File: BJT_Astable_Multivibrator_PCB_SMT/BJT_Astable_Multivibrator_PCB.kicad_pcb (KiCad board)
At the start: 2 copper layers, 7 parts

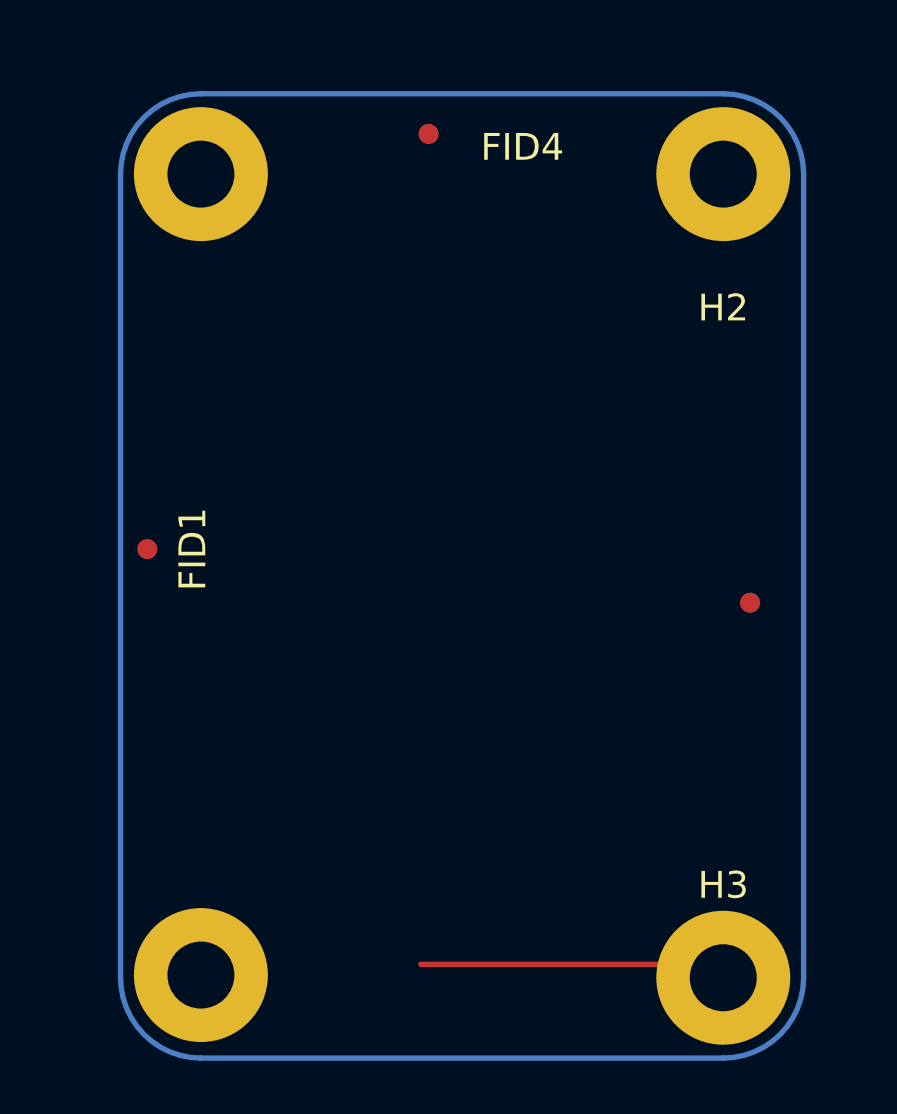
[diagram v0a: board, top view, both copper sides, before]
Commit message: added smt design of BJT mulitvibrator
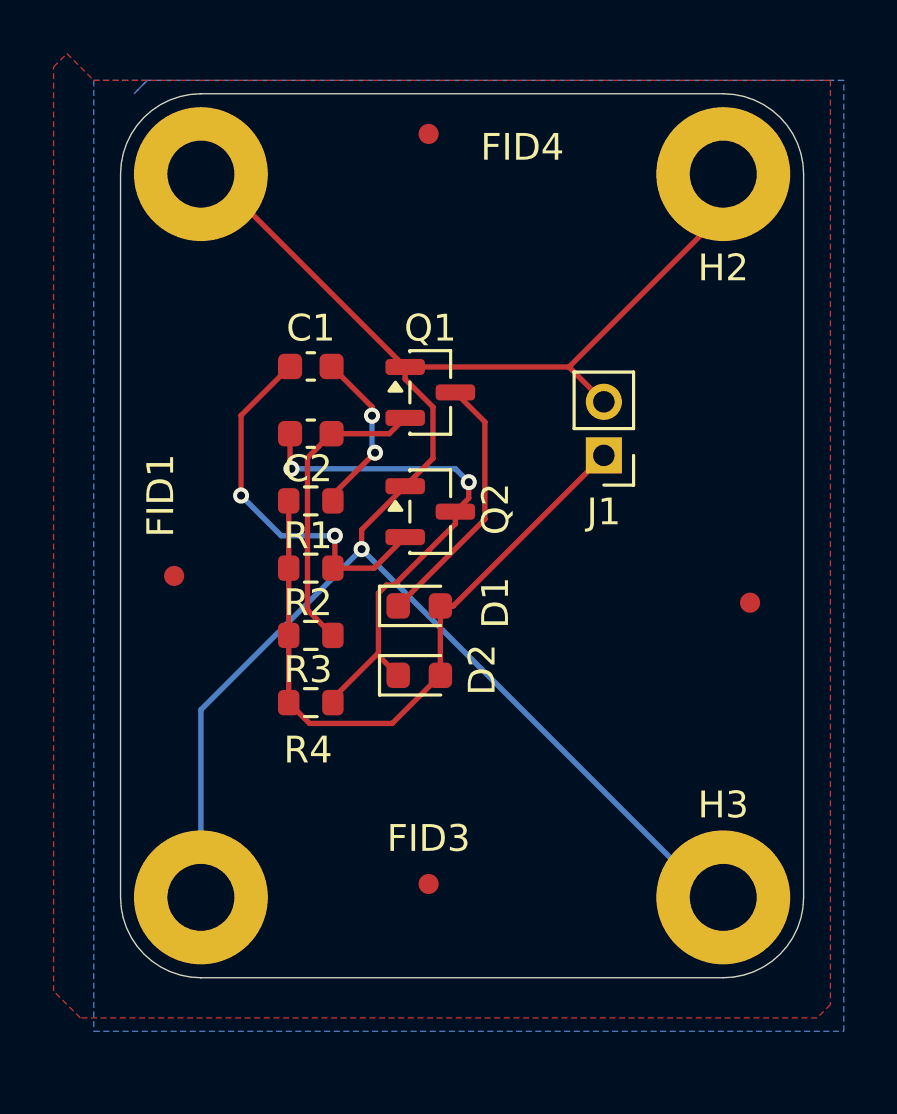
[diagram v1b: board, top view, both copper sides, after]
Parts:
- added C1: 220uF, Capacitor_SMD:C_0603_1608Metric, F.Cu at (150.6, 69.7)
- added C2: 220uF, Capacitor_SMD:C_0603_1608Metric, F.Cu at (150.6, 72.2)
- added D1: LED, LED_SMD:LED_0603_1608Metric, F.Cu at (154.7, 78.6)
- added D2: LED, LED_SMD:LED_0603_1608Metric, F.Cu at (154.7, 81.2)
- added FID3: Fiducial, Fiducial:Fiducial_0.75mm_Mask1.5mm, F.Cu at (155.0, 89.0)
- added J1: Conn_01x02_Pin, Connector_PinHeader_2.00mm:PinHeader_1x02_P2.00mm_Vertical, F.Cu at (161.5, 73.0)
- added Q1: 2N3904, Package_TO_SOT_SMD:SOT-23, F.Cu at (155.1, 70.7)
- added Q2: 2N3904, Package_TO_SOT_SMD:SOT-23, F.Cu at (155.1, 75.1)
- added R1: 1K, Resistor_SMD:R_0603_1608Metric, F.Cu at (150.6, 74.7)
- added R2: 5K, Resistor_SMD:R_0603_1608Metric, F.Cu at (150.6, 77.2)
- added R3: 5K, Resistor_SMD:R_0603_1608Metric, F.Cu at (150.6, 79.7)
- added R4: 1K, Resistor_SMD:R_0603_1608Metric, F.Cu at (150.6, 82.2)
- moved H3 3.00 mm to (166.0, 89.5)
- moved H4 2.90 mm to (146.5, 89.5)
- moved FID1 1.41 mm to (145.5, 77.5)
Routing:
- net GND: track 11.8 -> 70.9 mm, vias 0 -> 1
- net VCC: track 0.00 -> 25.3 mm
- net Net-(D2-K): track 0.00 -> 19.8 mm, vias 0 -> 2
- net Base2: track 0.00 -> 14.1 mm, vias 0 -> 2
- net Base1: track 0.00 -> 11.3 mm
- net Net-(D1-K): track 0.00 -> 9.77 mm
- net Net-(C1-Pad2): track 0.00 -> 6.34 mm, vias 0 -> 2
- added copper zone on B.Cu, net GND
- added copper zone on F.Cu, net GND
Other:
- board outline added: 25.5 x 33 mm
